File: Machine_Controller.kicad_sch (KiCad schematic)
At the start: 8 parts, among them J1 SERIAL, J2 DEBUG, J3 LCD, J4 RS485

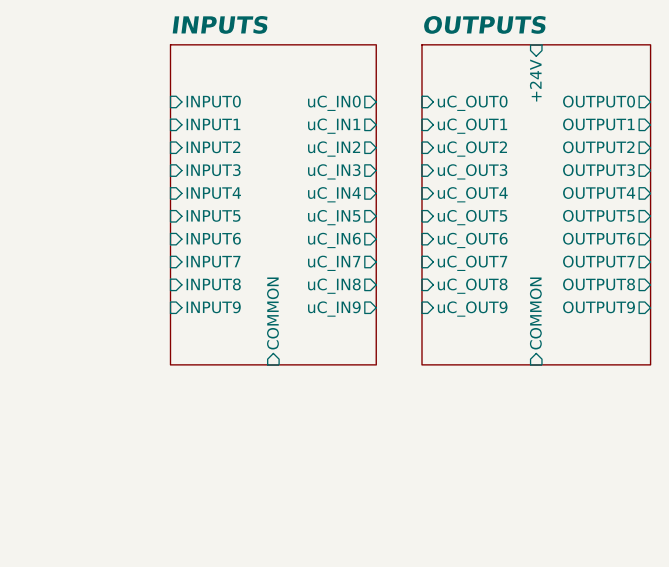
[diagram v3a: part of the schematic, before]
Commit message: Specefies which section is complete and incomplete
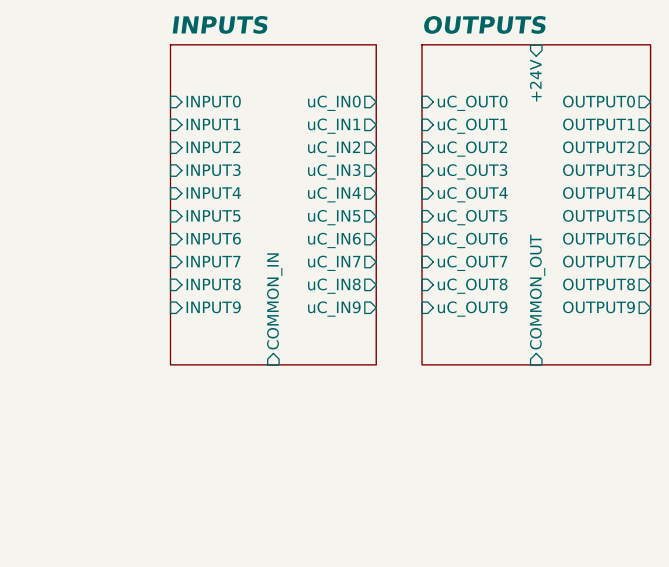
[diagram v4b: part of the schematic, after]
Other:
- sheet INPUTS ports: added COMMON_IN; removed COMMON
- sheet OUTPUTS ports: added COMMON_OUT; removed COMMON
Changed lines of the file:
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@@
+			)
+		)
+		(pin "OUTPUT0" output
+			(at 243.84 71.12 0)
+			(effects
+				(font
+					(size 1.27 1.27)
+				)
+				(justify right)
+			)
+		)
+		(pin "OUTPUT1" output
+			(at 243.84 73.66 0)
+			(effects
+				(font
+					(size 1.27 1.27)
+				)
+				(justify right)
+			)
+		)
+		(pin "OUTPUT2" output
+			(at 243.84 76.2 0)
+			(effects
+				(font
+					(size 1.27 1.27)
+				)
+				(justify right)
+			)
+		)
+		(pin "OUTPUT3" output
+			(at 243.84 78.74 0)
+			(effects
+				(font
+					(size 1.27 1.27)
+				)
+				(justify right)
+			)
+		)
+		(pin "OUTPUT4" output
+			(at 243.84 81.28 0)
+			(effects
+				(font
+					(size 1.27 1.27)
+				)
+				(justify right)
+			)
+		)
+		(pin "OUTPUT5" output
+			(at 243.84 83.82 0)
+			(effects
+				(font
+					(size 1.27 1.27)
+				)
+				(justify right)
+			)
+		)
+		(pin "OUTPUT6" output
+			(at 243.84 86.36 0)
+			(effects
+				(font
+					(size 1.27 1.27)
+				)
+				(justify right)
+			)
+		)
+		(pin "OUTPUT7" output
+			(at 243.84 88.9 0)
+			(effects
+				(font
+					(size 1.27 1.27)
+				)
+				(justify right)
+			)
+		)
+		(pin "OUTPUT8" output
+			(at 243.84 91.44 0)
+			(effects
+				(font
+					(size 1.27 1.27)
+				)
+				(justify right)
+			)
+		)
+		(pin "OUTPUT9" output
+			(at 243.84 93.98 0)
+			(effects
+				(font
+					(size 1.27 1.27)
+				)
+				(justify right)
+			)
+		)
+		(pin "uC_OUT0" input
+			(at 218.44 71.12 180)
+			(effects
+				(font
+					(size 1.27 1.27)
+				)
+				(justify left)
+			)
+		)
+		(pin "uC_OUT1" input
+			(at 218.44 73.66 180)
+			(effects
+				(font
+					(size 1.27 1.27)
+				)
+				(justify left)
+			)
+		)
+		(pin "uC_OUT2" input
+			(at 218.44 76.2 180)
+			(effects
+				(font
+					(size 1.27 1.27)
+				)
+				(justify left)
+			)
+		)
+		(pin "uC_OUT3" input
+			(at 218.44 78.74 180)
+			(effects
+				(font
+					(size 1.27 1.27)
+				)
+				(justify left)
+			)
+		)
+		(pin "uC_OUT4" input
+			(at 218.44 81.28 180)
+			(effects
+				(font
+					(size 1.27 1.27)
+				)
+				(justify left)
+			)
+		)
+		(pin "uC_OUT5" input
+			(at 218.44 83.82 180)
+			(effects
+				(font
+					(size 1.27 1.27)
+				)
+				(justify left)
+			)
+		)
+		(pin "uC_OUT6" input
+			(at 218.44 86.36 180)
+			(effects
+				(font
+					(size 1.27 1.27)
+				)
+				(justify left)
+			)
+		)
+		(pin "uC_OUT7" input
+			(at 218.44 88.9 180)
+			(effects
+				(font
+					(size 1.27 1.27)
+				)
+				(justify left)
+			)
+		)
+		(pin "uC_OUT8" input
+			(at 218.44 91.44 180)
+			(effects
+				(font
+					(size 1.27 1.27)
+				)
+				(justify left)
+			)
+		)
+		(pin "uC_OUT9" input
+			(at 218.44 93.98 180)
+			(effects
+				(font
+					(size 1.27 1.27)
+				)
+				(justify left)
 			)
 		)
@@
 			)
 		)
-		(pin "COMMON" input
+		(pin "COMMON_OUT" input
 			(at 231.14 100.33 270)
-			(effects
-				(font
-					(size 1.27 1.27)
-				)
-				(justify left)
-			)
-		)
-		(pin "OUTPUT0" output
-			(at 243.84 71.12 0)
-			(effects
-				(font
-					(size 1.27 1.27)
-				)
-				(justify right)
-			)
-		)
-		(pin "OUTPUT1" output
-			(at 243.84 73.66 0)
-			(effects
-				(font
-					(size 1.27 1.27)
-				)
-				(justify right)
-			)
-		)
-		(pin "OUTPUT2" output
-			(at 243.84 76.2 0)
-			(effects
-				(font
-					(size 1.27 1.27)
-				)
-				(justify right)
-			)
-		)
-		(pin "OUTPUT3" output
-			(at 243.84 78.74 0)
-			(effects
-				(font
-					(size 1.27 1.27)
-				)
-				(justify right)
-			)
-		)
-		(pin "OUTPUT4" output
-			(at 243.84 81.28 0)
-			(effects
-				(font
-					(size 1.27 1.27)
-				)
-				(justify right)
-			)
-		)
-		(pin "OUTPUT5" output
-			(at 243.84 83.82 0)
-			(effects
-				(font
-					(size 1.27 1.27)
-				)
-				(justify right)
-			)
-		)
-		(pin "OUTPUT6" output
-			(at 243.84 86.36 0)
-			(effects
-				(font
-					(size 1.27 1.27)
-				)
-				(justify right)
-			)
-		)
-		(pin "OUTPUT7" output
-			(at 243.84 88.9 0)
-			(effects
-				(font
-					(size 1.27 1.27)
-				)
-				(justify right)
-			)
-		)
-		(pin "OUTPUT8" output
-			(at 243.84 91.44 0)
-			(effects
-				(font
-					(size 1.27 1.27)
-				)
-				(justify right)
-			)
-		)
-		(pin "OUTPUT9" output
-			(at 243.84 93.98 0)
-			(effects
-				(font
-					(size 1.27 1.27)
-				)
-				(justify right)
-			)
-		)
-		(pin "uC_OUT0" input
-			(at 218.44 71.12 180)
-			(effects
-				(font
-					(size 1.27 1.27)
-				)
-				(justify left)
-			)
-		)
-		(pin "uC_OUT1" input
-			(at 218.44 73.66 180)
-			(effects
-				(font
-					(size 1.27 1.27)
-				)
-				(justify left)
-			)
-		)
-		(pin "uC_OUT2" input
-			(at 218.44 76.2 180)
-			(effects
-				(font
-					(size 1.27 1.27)
-				)
-				(justify left)
-			)
-		)
-		(pin "uC_OUT3" input
-			(at 218.44 78.74 180)
-			(effects
-				(font
-					(size 1.27 1.27)
-				)
-				(justify left)
-			)
-		)
-		(pin "uC_OUT4" input
-			(at 218.44 81.28 180)
-			(effects
-				(font
-					(size 1.27 1.27)
-				)
-				(justify left)
-			)
-		)
-		(pin "uC_OUT5" input
-			(at 218.44 83.82 180)
-			(effects
-				(font
-					(size 1.27 1.27)
-				)
-				(justify left)
-			)
-		)
-		(pin "uC_OUT6" input
-			(at 218.44 86.36 180)
-			(effects
-				(font
-					(size 1.27 1.27)
-				)
-				(justify left)
-			)
-		)
-		(pin "uC_OUT7" input
-			(at 218.44 88.9 180)
-			(effects
-				(font
-					(size 1.27 1.27)
-				)
-				(justify left)
-			)
-		)
-		(pin "uC_OUT8" input
-			(at 218.44 91.44 180)
-			(effects
-				(font
-					(size 1.27 1.27)
-				)
-				(justify left)
-			)
-		)
-		(pin "uC_OUT9" input
-			(at 218.44 93.98 180)
 			(effects
 				(font
@@
 			)
 		)
-		(pin "COMMON" input
-			(at 201.93 100.33 270)
-			(effects
-				(font
-					(size 1.27 1.27)
-				)
-				(justify left)
-			)
-		)
 		(pin "INPUT0" input
 			(at 190.5 71.12 180)
@@
 			)
 		)
+		(pin "COMMON_IN" input
+			(at 201.93 100.33 270)
+			(effects
+				(font
+					(size 1.27 1.27)
+				)
+				(justify left)
+			)
+		)
